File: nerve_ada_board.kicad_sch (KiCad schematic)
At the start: 51 parts, among them J1 TC2050-IDC, J2 USB-C Power Only 6P, J3 Camera, J4 CAN2, J5 CAN2, SW1 SPST, SW2 SPST, SW3 SPDT, SW4 SPST, U1 LD1117S33TR_SOT223, U2 XBP9B-DMWT-002, U3 STM32F446RET, U4 SAM-M10Q, Y1 8M, Y2 32.768K

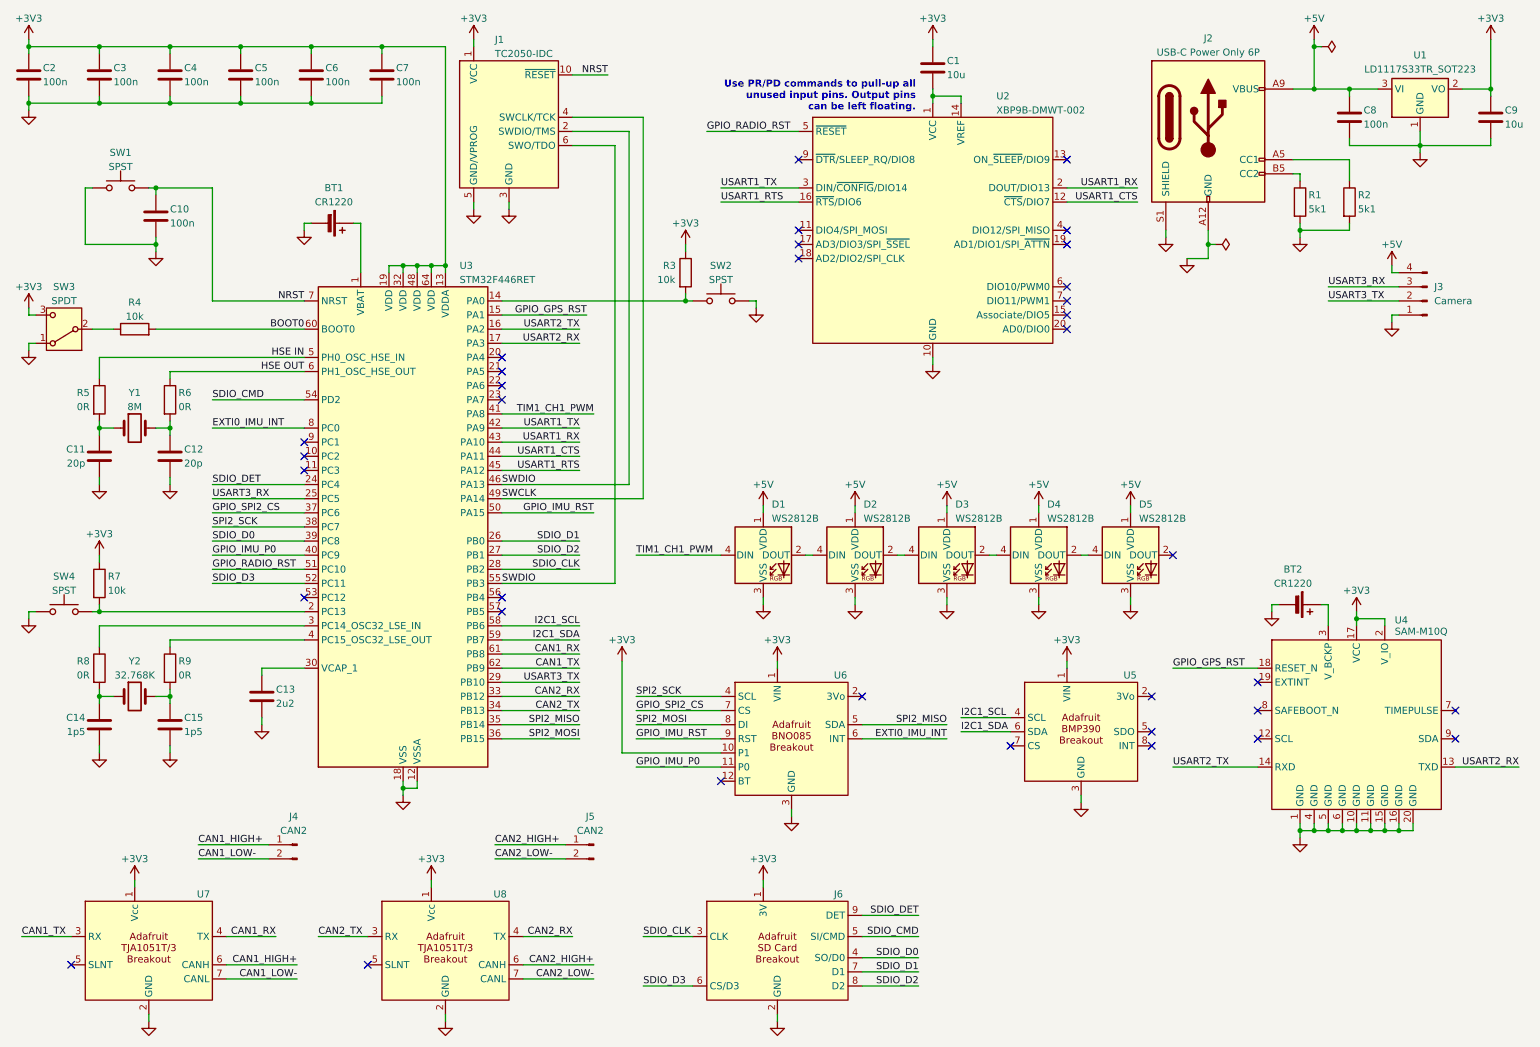
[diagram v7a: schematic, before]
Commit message: Add level shifter and buzzer, organize schematic
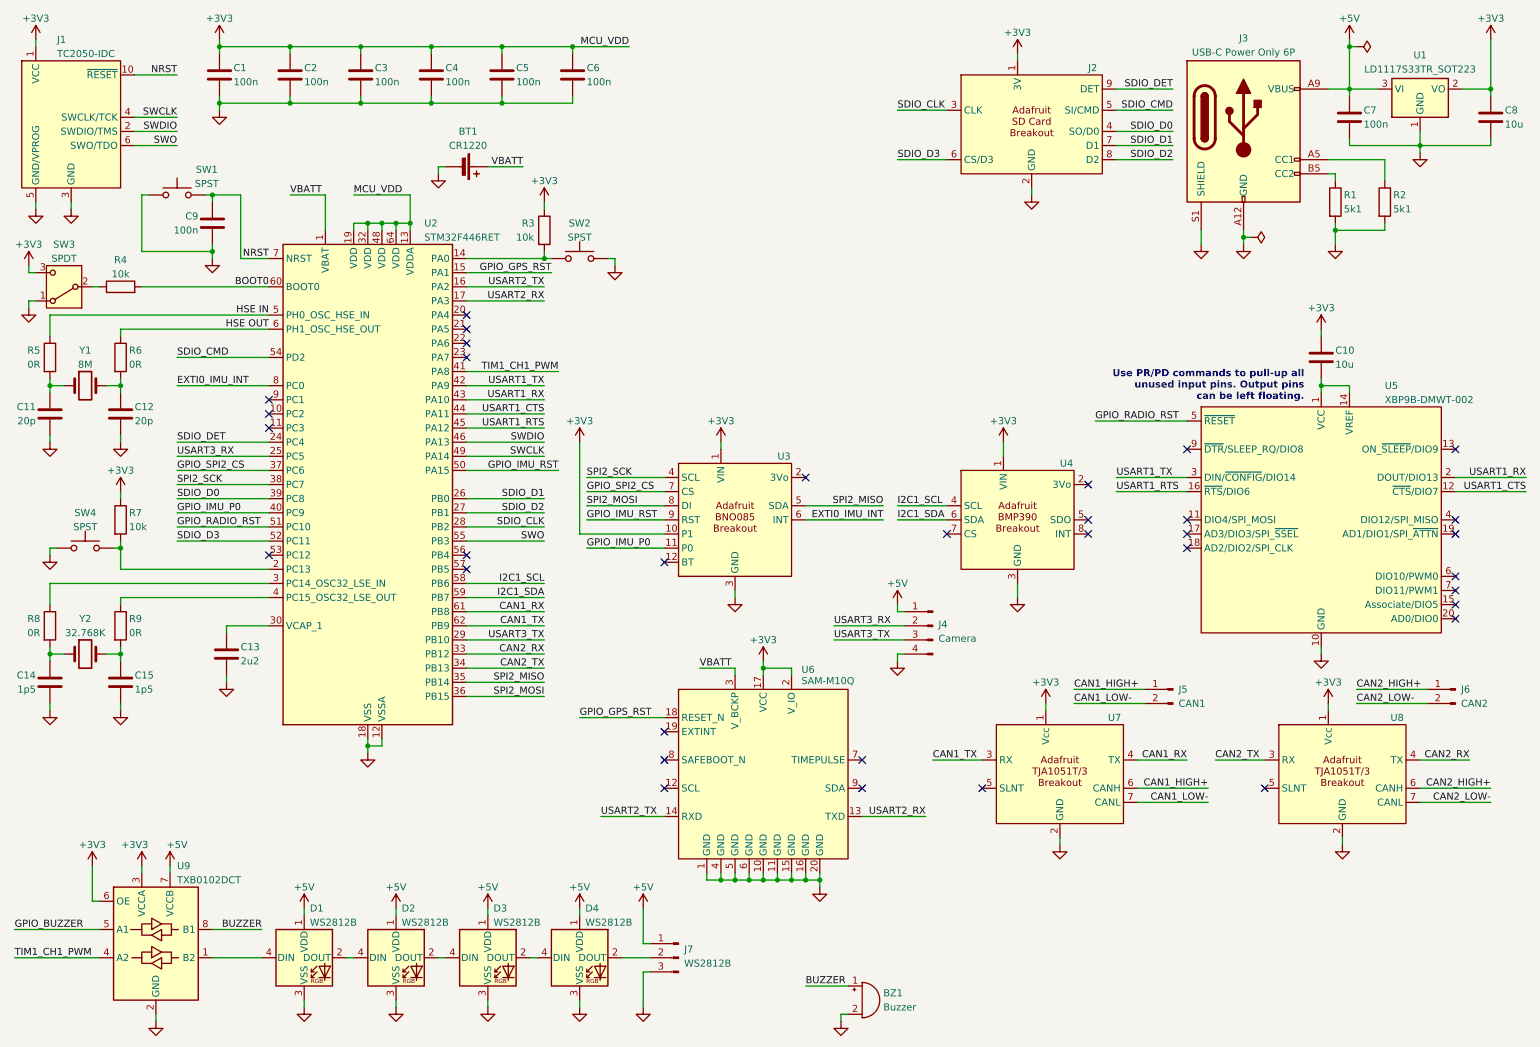
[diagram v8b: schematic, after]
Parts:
- removed BT2: CR1220, symbol Device:Battery_Cell
- removed D5: WS2812B, LED_SMD:LED_WS2812B_PLCC4_5.0x5.0mm_P3.2mm, symbol LED:WS2812B
- removed J3: Camera, symbol Connector:Conn_01x04_Pin
- added BZ1: Buzzer, symbol Device:Buzzer
- added J4: Camera, symbol Connector:Conn_01x04_Pin
- added J7: WS2812B, symbol Connector:Conn_01x03_Pin
- added U9: TXB0102DCT, Package_SO:TSSOP-8_3x3mm_P0.65mm, symbol Logic_LevelTranslator:TXB0102DCT
- J5: renamed from J4; value CAN2 -> CAN1
- renumbered C2 to C1, C1 to C10, C3 to C2, C4 to C3, C5 to C4, C6 to C5, C7 to C6, C8 to C7, C9 to C8, C10 to C9, J6 to J2, J2 to J3, J5 to J6, U3 to U2, U6 to U3, U5 to U4, U2 to U5, U4 to U6
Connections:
- net +3V3: now also U9.3 (VCCA), U9.6 (OE)
- net +5V: now also J4.1 (Pin_1), J7.1 (Pin_1), U9.7 (VCCB)
- net GND: now also BZ1.2 (-), J4.4 (Pin_4), J7.3 (Pin_3), U9.2 (GND)
- net SWDIO: no longer J1.6 (SWO/TDO), U2.55 (PB3)
- net TIM1_CH1_PWM: now also U9.4 (A2); no longer D1.4 (DIN)
- net USART3_RX: now also J4.2 (Pin_2)
- net USART3_TX: now also J4.3 (Pin_3)
- net VBATT: now reaches BT1.1 (+), U2.1 (VBAT)
- net VBATT: now also U6.3 (V_BCKP)
- net at D4.2 (DOUT): now also J7.2 (Pin_2)
- new net: D1.4 (DIN), U9.1 (B2)
- new net BUZZER: BZ1.1 (+), U9.8 (B1)
- new net GPIO_BUZZER: U9.5 (A1)
- new net SWO: J1.6 (SWO/TDO), U2.55 (PB3)
- no-connect marks 35 -> 34
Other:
- moved on the sheet: C1, C10, C11, C12, C13, C14, C15, C2, C3, C4, C5, C6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
